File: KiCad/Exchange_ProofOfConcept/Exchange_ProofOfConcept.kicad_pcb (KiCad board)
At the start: 2 copper layers, 94 x 99.1 mm, 57 parts, among them J1 Connector_PinHeader_2.54mm:Pi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, J2 Conn_01x02, J3 Conn_01x02, J4 Conn_01x02, J5 Connector_PinHeader_2.54mm:Pi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, J6 Connector_PinHeader_2.54mm:Pi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, J7 Screw_Terminal_01x02, J8 Conn_01x03, J9 Screw_Terminal_01x08, U1 MCP23017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

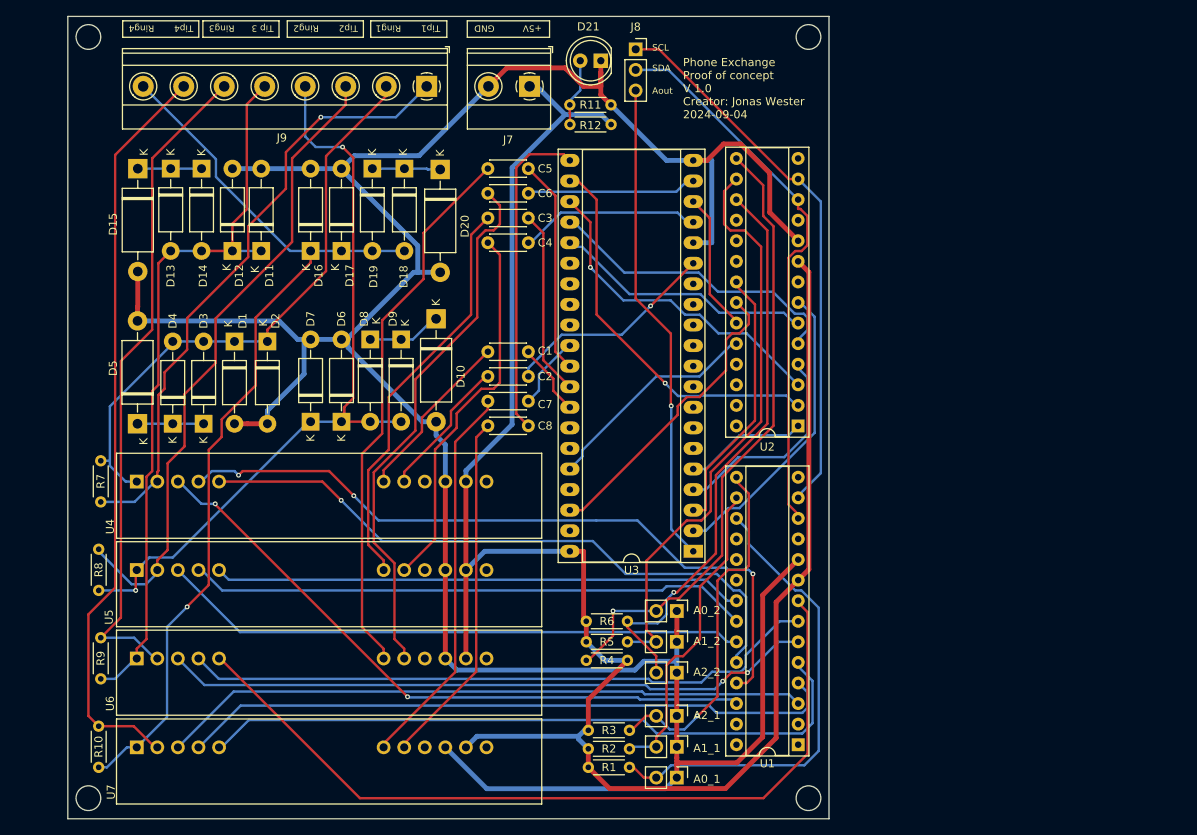
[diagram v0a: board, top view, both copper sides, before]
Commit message: deleted:    KiCad/Exchange_ProofOfConcept/Exchange_ProofOfConcept-backups/Exchange_ProofOfConcept-2024-08-28_233227.zip 	deleted:    KiCad/Exchange_ProofOfConcept/Exchange_ProofOfConcept-backups/Exchange_ProofOfConcept-2024-08-28_234504.zip 	deleted:    KiCad/Exchange_ProofOfConcept/Exchange_ProofOfConcept-backups/Exchange_ProofOfConcept-2024-09-04_201626.zip 	deleted:    KiCad/Exchange_ProofOfConcept/Exchange_ProofOfConcept-backups/Exchange_ProofOfConcept-2024-09-04_202659.zip 	deleted:    KiCad/Exchange_ProofOfConcept/Exchange_ProofOfConcept-backups/Exchange_ProofOfConcept-2024-09-04_203703.zip 	deleted:    KiCad/Exchange_ProofOfConcept/Exchange_ProofOfConcept-backups/Exchange_ProofOfConcept-2024-09-04_204710.zip 	deleted:    KiCad/Exchange_ProofOfConcept/Exchange_ProofOfConcept-backups/Exchange_ProofOfConcept-2024-09-04_205754.zip 	deleted:    KiCad/Exchange_ProofOfConcept/Exchange_ProofOfConcept-backups/Exchange_ProofOfConcept-2024-09-05_153643.zip 	deleted:    KiCad/Exchange_ProofOfConcept/Exchange_ProofOfConcept-backups/Exchange_ProofOfConcept-2024-09-05_161017.zip 	deleted:    KiCad/Exchange_ProofOfConcept/Exchange_ProofOfConcept-backups/Exchange_ProofOfConcept-2024-09-05_162441.zip 	deleted:    KiCad/Exchange_ProofOfConcept/Exchange_ProofOfConcept-backups/Exchange_ProofOfConcept-2024-09-05_163641.zip 	deleted:    KiCad/Exchange_ProofOfConcept/Exchange_ProofOfConcept-backups/Exchange_ProofOfConcept-2024-09-06_180233.zip 	deleted:    KiCad/Exchange_ProofOfConcept/Exchange_ProofOfConcept-backups/Exchange_ProofOfConcept-2024-09-06_180943.zip 	deleted:    KiCad/Exchange_ProofOfConcept/Exchange_ProofOfConcept-backups/Exchange_ProofOfConcept-2024-09-06_182256.zip 	deleted:    KiCad/Exchange_ProofOfConcept/Exchange_ProofOfConcept-backups/Exchange_ProofOfConcept-2024-09-06_185314.zip 	deleted:    KiCad/Exchange_ProofOfConcept/Exchange_ProofOfConcept-backups/Exchange_ProofOfConcept-2024-09-06_191143.zip 	deleted:    KiCad/Exchange_ProofOfConcept/Exchange_ProofOfConcep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
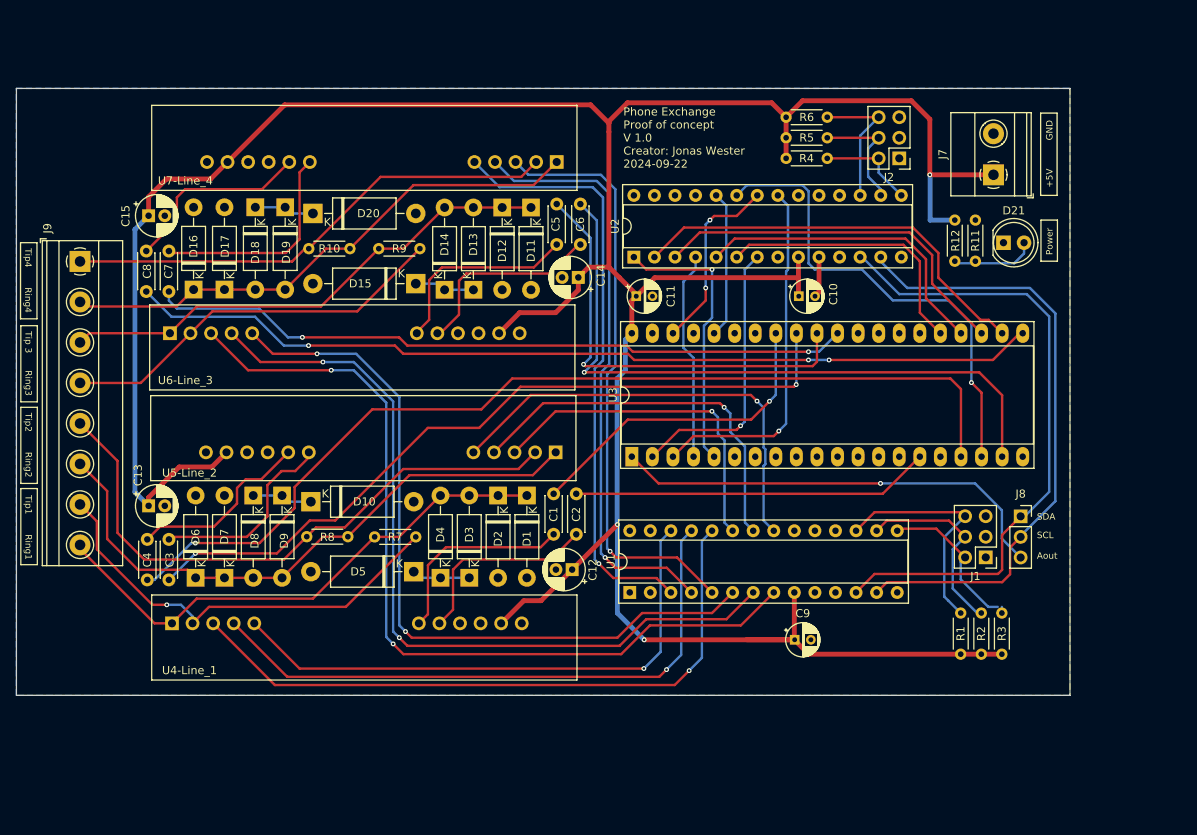
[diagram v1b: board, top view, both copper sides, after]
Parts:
- removed J3, J4: Conn_01x02, Connector_PinHeader_2.54mm:PinHeader_1x02_P2.54mm_Vertical
- removed J5, J6: Connector_PinHeader_2.54mm:PinHeader_1x02_P2.54mm_Vertical, Connector_PinHeader_2.54mm:PinHeader_1x02_P2.54mm_Vertical
- removed U4, U5, U6, U7: ~, JW_footprint_library:KS0835F
- added C10: 10uF, Capacitor_THT:CP_Radial_D4.0mm_P2.00mm, F.Cu at (172.8, 76.5)
- added C11: 10uF, Capacitor_THT:CP_Radial_D4.0mm_P2.00mm, F.Cu at (152.7, 76.5)
- added C12: 100uF, Capacitor_THT:CP_Radial_D5.0mm_P2.00mm, F.Cu at (144.8, 110.2)
- added C13: 100uF, Capacitor_THT:CP_Radial_D5.0mm_P2.00mm, F.Cu at (92.5, 102.3)
- added C14: 100uF, Capacitor_THT:CP_Radial_D5.0mm_P2.00mm, F.Cu at (145.6, 74.1)
- added C15: 100uF, Capacitor_THT:CP_Radial_D5.0mm_P2.00mm, F.Cu at (92.5, 66.5)
- added C9: 10uF, Capacitor_THT:CP_Radial_D4.0mm_P2.00mm, F.Cu at (172.3, 118.9)
- added U4-Line_1: ~, JW_footprint_library:KS0835F, F.Cu at (95.4, 116.8)
- added U5-Line_2: ~, JW_footprint_library:KS0835F, F.Cu at (142.8, 95.7)
- added U6-Line_3: ~, JW_footprint_library:KS0835F, F.Cu at (95.2, 81.0)
- added U7-Line_4: ~, JW_footprint_library:KS0835F, F.Cu at (142.9, 59.9)
- J1: value Connector_PinHeader_2.54mm:PinHeader_1x02_P2.54mm_Vertical -> Conn_02x03_Odd_Even; footprint Connector_PinHeader_2.54mm:PinHeader_1x02_P2.54mm_Vertical -> Connector_PinHeader_2.54mm:PinHeader_2x03_P2.54mm_Vertical
- J2: value Conn_01x02 -> Conn_02x03_Odd_Even; footprint Connector_PinHeader_2.54mm:PinHeader_1x02_P2.54mm_Vertical -> Connector_PinHeader_2.54mm:PinHeader_2x03_P2.54mm_Vertical
- moved J2 77.7 mm to (185.2, 59.4), turned to 180 degrees
- moved J8 74.7 mm to (200.2, 103.6)
- moved R10 71.2 mm to (117.4, 70.6), turned to 180 degrees
- moved R5 66.9 mm to (171.2, 56.9)
- moved R6 66.9 mm to (171.2, 54.4)
- moved R4 65.0 mm to (171.2, 59.4), turned to 0 degrees
- moved R9 63.2 mm to (120.9, 70.6), turned to 0 degrees
- moved J7 58.3 mm to (196.8, 61.5), turned to 90 degrees
- moved C3 55.9 mm to (95.0, 106.5), turned to -90 degrees
- moved C4 55.8 mm to (92.4, 106.5), turned to -90 degrees
- moved D21 54.6 mm to (198.1, 69.8), turned to 0 degrees
- moved R3 51.9 mm to (197.9, 120.7), turned to 90 degrees
- moved R2 49.9 mm to (195.3, 120.7), turned to 90 degrees
- moved R1 48.0 mm to (192.8, 120.7), turned to 90 degrees
- moved J9 47.9 mm to (84.1, 72.2), turned to -90 degrees
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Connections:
- J8 pad 1: /SCL -> /SDA
- J8 pad 2: /SDA -> /SCL
- J9 pad 1: /TIP_1 -> /TIP_4
- J9 pad 2: /RING_1 -> /RING_4
- J9 pad 3: /TIP_2 -> /TIP_3
- J9 pad 4: /RING_2 -> /RING_3
- J9 pad 5: /TIP_3 -> /TIP_2
- J9 pad 6: /RING_3 -> /RING_2
- J9 pad 7: /TIP_4 -> /TIP_1
- J9 pad 8: /RING_4 -> /RING_1
- R1 pad 2: Net-(J1-Pin_2) -> Net-(J1-Pin_6)
- R2 pad 2: Net-(J2-Pin_2) -> Net-(J1-Pin_4)
- R3 pad 2: Net-(J3-Pin_2) -> Net-(J1-Pin_2)
- R4 pad 2: Net-(J4-Pin_2) -> Net-(J2-Pin_2)
- R5 pad 2: Net-(J5-Pin_2) -> Net-(J2-Pin_4)
- R6 pad 2: Net-(J6-Pin_2) -> Net-(J2-Pin_6)
- U1 pad 15: Net-(J3-Pin_2) -> Net-(J1-Pin_2)
- U1 pad 16: Net-(J2-Pin_2) -> Net-(J1-Pin_4)
- U1 pad 17: Net-(J1-Pin_2) -> Net-(J1-Pin_6)
- U1 pad 24: /SLIC 1/SHK_1 -> /SLIC 1/FR_1
- U1 pad 26: /SLIC 1/FR_1 -> /SLIC 1/SHK_1
- U1 pad 3: /SLIC 4/FR_4 -> /SLIC 4/SHK_4
- U1 pad 5: /SLIC 4/SHK_4 -> /SLIC 4/FR_4
- U1 pad 6: /SLIC 3/FR_3 -> /SLIC 3/SHK_3
- U1 pad 8: /SLIC 3/SHK_3 -> /SLIC 3/FR_3
- U2 pad 15: Net-(J4-Pin_2) -> Net-(J2-Pin_2)
- U2 pad 16: Net-(J5-Pin_2) -> Net-(J2-Pin_4)
- U2 pad 17: Net-(J6-Pin_2) -> Net-(J2-Pin_6)
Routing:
- net GND: track 352.0 -> 5.04 mm
- net /5V: track 236.0 -> 374.1 mm, vias 0 -> 3
- net /Aout_2: track 22.4 -> 121.2 mm, vias 0 -> 1
- net /Ain_4: track 9.13 -> 87.2 mm, vias 0 -> 2
- net Net-(J4-Pin_2): track 77.5 -> 0.00 mm, vias 1 -> 0
- net /Aout_4: track 40.1 -> 113.1 mm, vias 0 -> 3
- net Net-(J5-Pin_2): track 71.7 -> 0.00 mm
- net Net-(J6-Pin_2): track 71.0 -> 0.00 mm, vias 1 -> 0
- net /Ain_2: track 22.9 -> 93.8 mm, vias 0 -> 2
- net /Aout_3: track 21.0 -> 82.6 mm, vias 0 -> 1
- net /RING_4: track 117.8 -> 66.9 mm, vias 1 -> 0
- net Net-(J3-Pin_2): track 44.6 -> 0.00 mm, vias 1 -> 0
- net Net-(U6-Line_3-Audio_in): track 68.0 -> 24.8 mm
- net Net-(U6-Line_3-Audio_out): track 66.6 -> 24.6 mm
- net Net-(U2-GPA2): track 17.2 -> 58.8 mm, vias 0 -> 1
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- added copper zone on B.Cu, net GND
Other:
- board size 94 x 99.1 mm -> 130.1 x 74.9 mm
- board text added: "Phone Exchange Proof of concept V 1.0 Creator: Jonas Wester 2024-09-22"
- board text added: "Power"
- board text removed: "A0_1"
- board text removed: "A0_2"
- board text removed: "A1_1"
- board text removed: "A1_2"
- board text removed: "A2_1"
- board text removed: "A2_2"
- board text removed: "Phone Exchange Proof of concept V 1.0 Creator: Jonas Wester 2024-09-04"

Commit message: deleted:    KiCad/Exchange_ProofOfConcept/Exchange_ProofOfConcept-backups/Exchange_ProofOfConcept-2024-09-22_003036.zip 	deleted:    KiCad/Exchange_ProofOfConcept/Exchange_ProofOfConcept-backups/Exchange_ProofOfConcept-2024-09-22_004107.zip 	deleted:    KiCad/Exchange_ProofOfConcept/Exchange_ProofOfConcept-backups/Exchange_ProofOfConcept-2024-09-22_004744.zip 	new file:   KiCad/Exchange_ProofOfConcept/Exchange_ProofOfConcept-backups/Exchange_ProofOfConcept-2024-09-22_093037.zip 	new file:   KiCad/Exchange_ProofOfConcept/Exchange_ProofOfConcept-backups/Exchange_ProofOfConcept-2024-09-22_093847.zip 	new file:   KiCad/Exchange_ProofOfConcept/Exchange_ProofOfConcept-backups/Exchange_ProofOfConcept-2024-09-22_094927.zip 	modified:   KiCad/Exchange_ProofOfConcept/Exchange_ProofOfConcept.kicad_pcb 	modified:   KiCad/Exchange_ProofOfConcept/Exchange_ProofOfConcept.kicad_prl
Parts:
- moved D21 2.08 mm to (199.1, 68.1), turned to -90 degrees
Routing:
- net /5V: track 374.1 -> 369.8 mm
- net /SLIC 2/FR_2: track 42.3 -> 38.8 mm
- net /SLIC 2/RM_2: track 47.9 -> 44.4 mm
- net Net-(D21-A): track 10.7 -> 7.88 mm
- net Net-(U2-GPB1): track 51.6 -> 53.8 mm
- net Net-(U2-GPB2): track 46.3 -> 48.3 mm
- net Net-(U2-GPB4): track 38.8 -> 40.2 mm
- net /Ain_1: track 40.1 -> 41.3 mm
- net Net-(U2-GPB5): track 34.0 -> 34.8 mm
- net /SCL: track 76.7 -> 77.2 mm

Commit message: deleted:    KiCad/Exchange_ProofOfConcept/Exchange_ProofOfConcept-backups/Exchange_ProofOfConcept-2024-09-22_005249.zip 	new file:   KiCad/Exchange_ProofOfConcept/Exchange_ProofOfConcept-backups/Exchange_ProofOfConcept-2024-10-02_184119.zip 	modified:   KiCad/Exchange_ProofOfConcept/Exchange_ProofOfConcept.kicad_pcb 	modified:   KiCad/Exchange_ProofOfConcept/Exchange_ProofOfConcept.kicad_sch 	modified:   docs/PhoneStatusflowshart.drawio 	modified:   lib/LineStatusHandler/LineStatusHandler.cpp 	modified:   lib/LineStatusHandler/LineStatusHandler.h 	modified:   platformio.ini 	modified:   src/SHKRead.h 	modified:   src/config.h 	modified:   src/lineAction.h 	modified:   src/main.cpp
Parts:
- removed R11: 1K, Resistor_THT:R_Axial_DIN0204_L3.6mm_D1.6mm_P5.08mm_Horizontal
- R12: value 430 -> 470
- moved R12 2.51 mm to (194.6, 67.1)
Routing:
- net Net-(D21-A): track 7.88 -> 4.95 mm
- net /5V: track 369.8 -> 372.3 mm

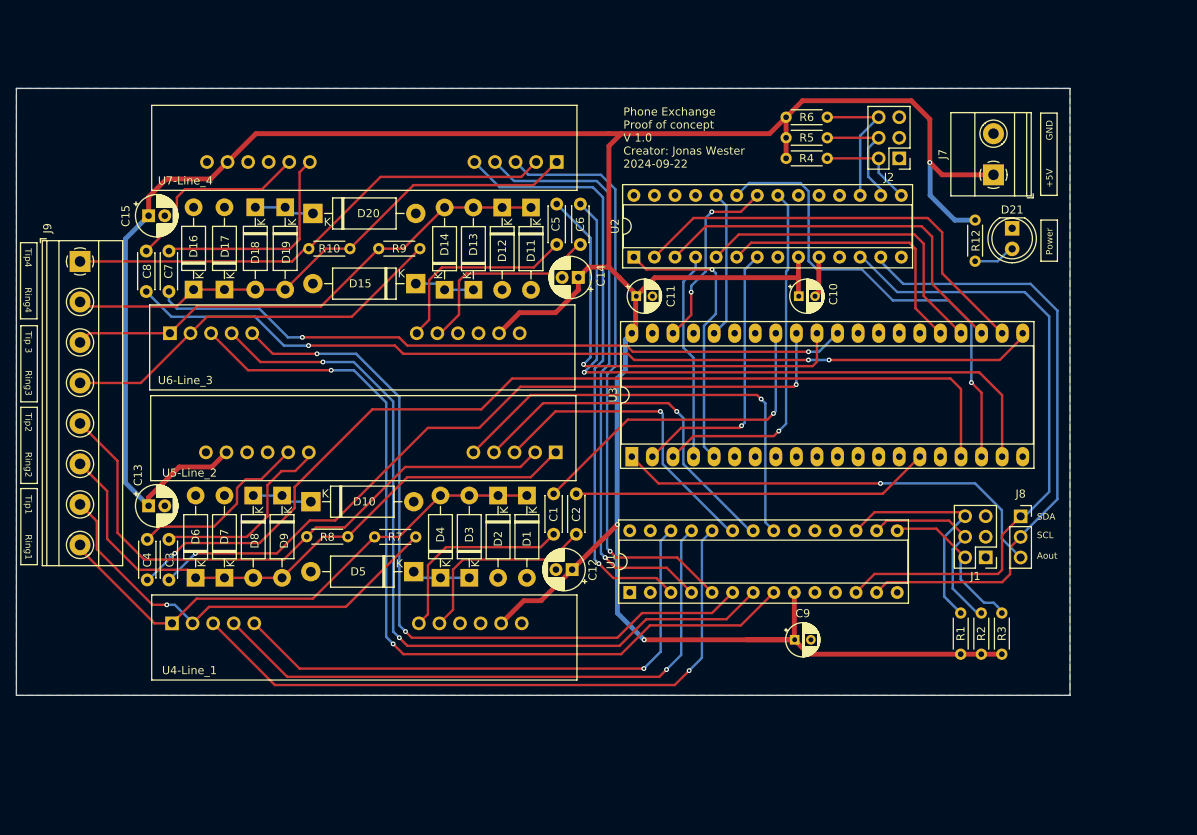
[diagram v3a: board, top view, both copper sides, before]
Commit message: deleted:    KiCad/Exchange_ProofOfConcept/Exchange_ProofOfConcept-backups/Exchange_ProofOfConcept-2024-09-09_184758.zip 	new file:   KiCad/Exchange_ProofOfConcept/Exchange_ProofOfConcept-backups/Exchange_ProofOfConcept-2024-10-06_223658.zip 	new file:   KiCad/Exchange_ProofOfConcept/Exchange_ProofOfConcept-backups/Exchange_ProofOfConcept-2024-10-10_194257.zip 	modified:   KiCad/Exchange_ProofOfConcept/Exchange_ProofOfConcept.kicad_pcb 	modified:   docs/PhoneStatusflowshart.drawio 	modified:   platformio.ini 	modified:   src/main.cpp
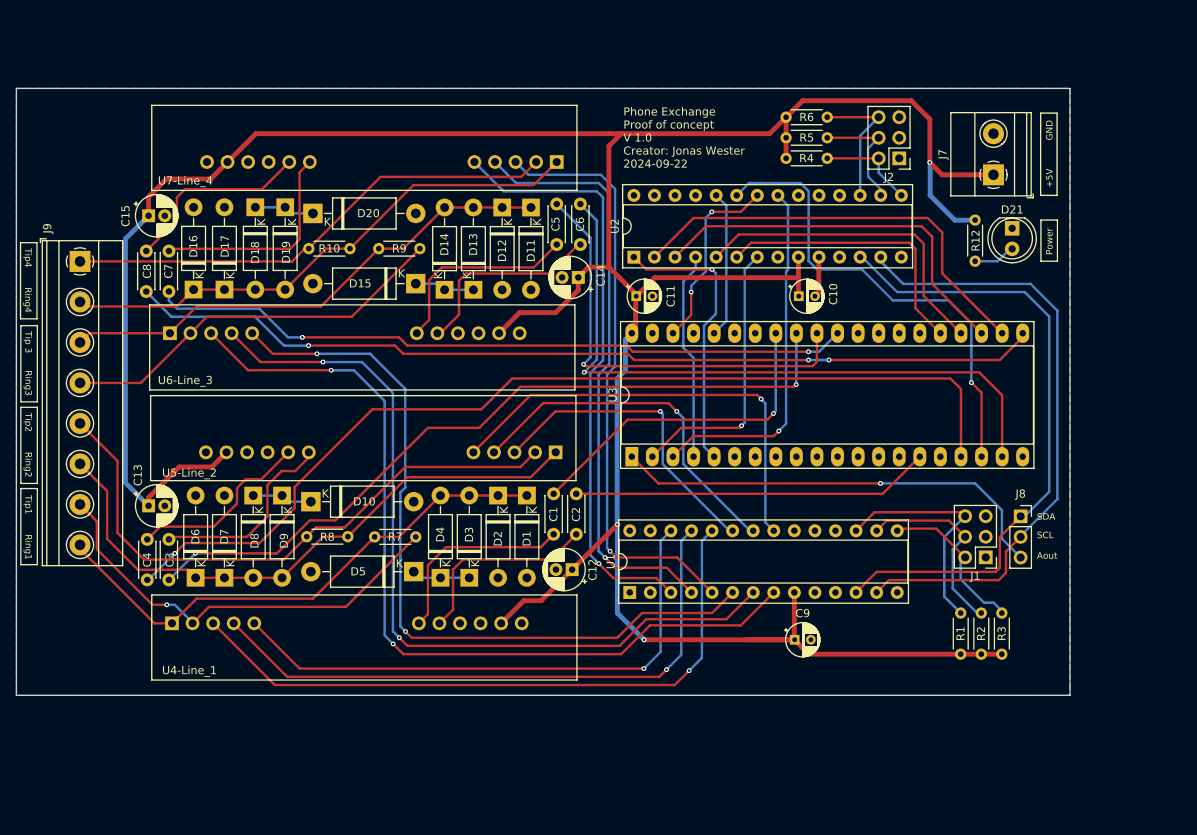
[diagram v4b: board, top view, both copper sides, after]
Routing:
- net /SLIC 3/SHK_3: track 93.7 -> 95.2 mm
- net /SLIC 3/RM_3: track 99.8 -> 100.3 mm

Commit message: new file:   KiCad/Exchange_ProofOfConcept/ESP-Unit/ESP-Unit-backups/ESP-Unit-2024-10-22_204833.zip 	new file:   KiCad/Exchange_ProofOfConcept/ESP-Unit/ESP-Unit-backups/ESP-Unit-2024-10-22_205851.zip 	new file:   KiCad/Exchange_ProofOfConcept/ESP-Unit/ESP-Unit-backups/ESP-Unit-2024-10-22_214835.zip 	new file:   KiCad/Exchange_ProofOfConcept/ESP-Unit/ESP-Unit-backups/ESP-Unit-2024-10-31_190638.zip 	new file:   KiCad/Exchange_ProofOfConcept/ESP-Unit/ESP-Unit.kicad_pcb 	new file:   KiCad/Exchange_ProofOfConcept/ESP-Unit/ESP-Unit.kicad_prl 	new file:   KiCad/Exchange_ProofOfConcept/ESP-Unit/ESP-Unit.kicad_pro 	new file:   KiCad/Exchange_ProofOfConcept/ESP-Unit/ESP-Unit.kicad_sch 	new file:   KiCad/Exchange_ProofOfConcept/ESP-Unit/fp-info-cache 	deleted:    KiCad/Exchange_ProofOfConcept/Exchange_ProofOfConcept-backups/Exchange_ProofOfConcept-2024-09-09_193050.zip 	deleted:    KiCad/Exchange_ProofOfConcept/Exchange_ProofOfConcept-backups/Exchange_ProofOfConcept-2024-09-10_220108.zip 	deleted:    KiCad/Exchange_ProofOfConcept/Exchange_ProofOfConcept-backups/Exchange_ProofOfConcept-2024-09-10_232037.zip 	deleted:    KiCad/Exchange_ProofOfConcept/Exchange_ProofOfConcept-backups/Exchange_ProofOfConcept-2024-09-11_034329.zip 	deleted:    KiCad/Exchange_ProofOfConcept/Exchange_ProofOfConcept-backups/Exchange_ProofOfConcept-2024-09-11_195456.zip 	deleted:    KiCad/Exchange_ProofOfConcept/Exchange_ProofOfConcept-backups/Exchange_ProofOfConcept-2024-09-17_174014.zip 	deleted:    KiCad/Exchange_ProofOfConcept/Exchange_ProofOfConcept-backups/Exchange_ProofOfConcept-2024-09-17_181112.zip 	deleted:    KiCad/Exchange_ProofOfConcept/Exchange_ProofOfConcept-backups/Exchange_ProofOfConcept-2024-09-19_202603.zip 	deleted:    KiCad/Exchange_ProofOfConcept/Exchange_ProofOfConcept-backups/Exchange_ProofOfConcept-2024-09-19_204637.zip 	deleted:    KiCad/Exchange_ProofOfConcept/Exchange_ProofOfConcept-backups/Exchange_ProofOfConcept-2024-09-19_205646.zip 	deleted:    KiCad/Exchange_ProofOfConcep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
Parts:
- removed J8: Conn_01x03, Connector_PinSocket_2.54mm:PinSocket_1x03_P2.54mm_Vertical
- added C16: 100nF, Capacitor_THT:C_Disc_D5.0mm_W2.5mm_P2.50mm, F.Cu at (178.6, 119.4)
- added C17: 100nF, Capacitor_THT:C_Disc_D5.0mm_W2.5mm_P2.50mm, F.Cu at (180.6, 76.2)
- added J3: Conn_01x04, Connector_PinSocket_2.54mm:PinSocket_1x04_P2.54mm_Vertical, F.Cu at (202.0, 102.1)
- added R11: 10K, Resistor_THT:R_Axial_DIN0207_L6.3mm_D2.5mm_P7.62mm_Horizontal, F.Cu at (191.3, 121.9)
- added R13: 10K, Resistor_THT:R_Axial_DIN0207_L6.3mm_D2.5mm_P7.62mm_Horizontal, F.Cu at (166.6, 60.5)
- added R14: 4,7K, Resistor_THT:R_Axial_DIN0207_L6.3mm_D2.5mm_P7.62mm_Horizontal, F.Cu at (211.6, 89.4)
- added R15: 4,7K, Resistor_THT:R_Axial_DIN0207_L6.3mm_D2.5mm_P7.62mm_Horizontal, F.Cu at (211.6, 93.5)
- R1, R10, R12, R2, R3, R4, R5, R6, R7, R8, R9: footprint Resistor_THT:R_Axial_DIN0204_L3.6mm_D1.6mm_P5.08mm_Horizontal -> Resistor_THT:R_Axial_DIN0207_L6.3mm_D2.5mm_P7.62mm_Horizontal
- moved R3 4.26 mm to (201.9, 121.9)
- moved R2 3.30 mm to (198.4, 121.9)
- moved R9 2.66 mm to (118.6, 71.9)
- moved C15 2.62 mm to (89.9, 66.8)
- moved R1 2.40 mm to (194.8, 121.9)
- moved C9 2.32 mm to (173.5, 116.9), turned to -90 degrees
- moved D9 1.81 mm to (107.2, 101.1)
- moved R12 1.80 mm to (193.3, 65.8)
- moved R10 1.58 mm to (118.4, 69.3)
- moved R4 1.56 mm to (169.7, 59.4)
- moved R5 1.56 mm to (169.7, 56.9)
- moved R6 1.56 mm to (169.7, 54.4)
- moved D8 1.56 mm to (103.9, 101.1)
- moved D19 1.43 mm to (108.0, 65.5)
- moved R7 1.40 mm to (119.1, 106.7)
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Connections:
- U1 pad 18: unconnected-(U1-~{RESET}-Pad18) -> Net-(U1-~{RESET})
- U1 pad 19: unconnected-(U1-INTB-Pad19) -> /SLIC INT
- U1 pad 20: unconnected-(U1-INTA-Pad20) -> /SLIC INT
- U2 pad 18: unconnected-(U2-~{RESET}-Pad18) -> Net-(U2-~{RESET})
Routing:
- net GND: track 5.04 -> 32.1 mm
- net Net-(U1-~{RESET}): track 0.00 -> 25.3 mm
- net Net-(U2-~{RESET}): track 0.00 -> 12.7 mm
- net /5V: track 372.3 -> 382.1 mm
- net Net-(U5-Line_2-Audio_out): track 23.0 -> 16.1 mm
- net Net-(U5-Line_2-Audio_in): track 24.6 -> 27.4 mm
- net /TIP_1: track 54.0 -> 56.0 mm
- net /Ain_2: track 93.8 -> 95.7 mm
- net /Ain_3: track 54.5 -> 56.4 mm
- net Net-(J1-Pin_2): track 19.8 -> 21.7 mm
- net Net-(D21-A): track 4.95 -> 6.75 mm
- net Net-(U7-Line_4-Audio_in): track 26.8 -> 25.2 mm
- net /Aout_3: track 82.6 -> 84.2 mm
- net Net-(D8-K): track 7.43 -> 8.98 mm
- net /Aout_x: track 55.2 -> 56.4 mm
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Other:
- board text added: "Phone Exchange Proof of concept V 1.0 Creator: Jonas Wester 2024-10-14"
- board text removed: "Phone Exchange Proof of concept V 1.0 Creator: Jonas Wester 2024-09-22"
